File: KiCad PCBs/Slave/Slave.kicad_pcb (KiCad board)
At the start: 2 copper layers, 73 x 55.9 mm, 46 parts, among them J1 Screw_Terminal_01x02, J10 AVR-ISP-6, J11 Conn_01x06_Female, J12 Screw_Terminal_01x02, J13 Screw_Terminal_01x02, J14 Screw_Terminal_01x02, J15 Screw_Terminal_01x02, J16 Screw_Terminal_01x02, J2 Screw_Terminal_01x02, J3 Screw_Terminal_01x02, J4 Screw_Terminal_01x02, J5 Screw_Terminal_01x02, J6 Screw_Terminal_01x02, J7 Screw_Terminal_01x02, J8 Screw_Terminal_01x02, J9 Screw_Terminal_01x02, SW1 SW_DIP_x02, SW2 SW_DIP_x02, SW3 SW_MEC_5E, U1 ATmega328P-AU, U2 MAX487ESA+T, U3 ULN2003A, U5 AMS1117-5.0, Y1 Crystal_GND24

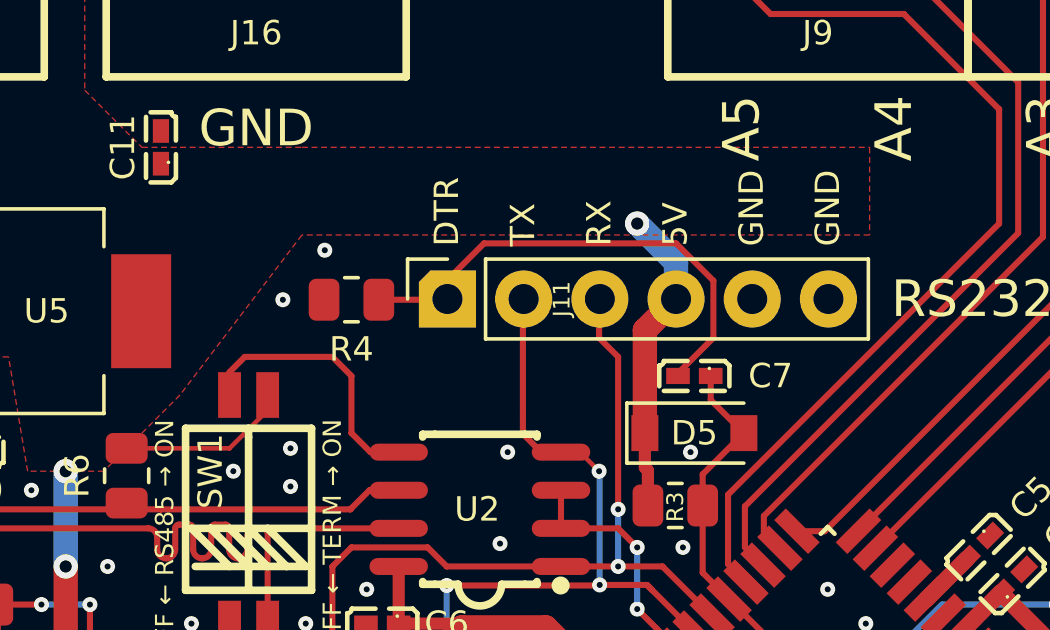
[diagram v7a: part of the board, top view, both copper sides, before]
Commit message: Removed unnecessary resistor
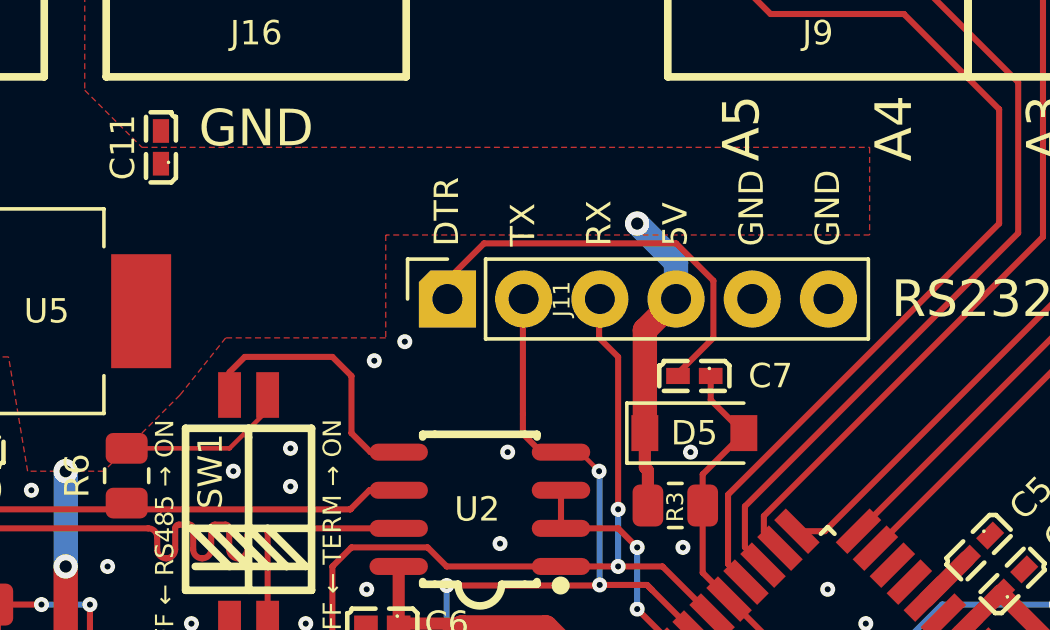
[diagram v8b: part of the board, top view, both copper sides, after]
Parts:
- removed R4: 1K, Resistor_SMD:R_0805_2012Metric
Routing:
- net FTDI_DTR: track 17.4 -> 14.7 mm
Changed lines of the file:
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@@
-    )
-  )
-  (footprint "Resistor_SMD:R_0805_2012Metric" (layer "F.Cu")
-    (at 133.985 91.4396 180)
-    (descr "Resistor SMD 0805 (2012 Metric), square (rectangular) end terminal, IPC_7351 nominal, (Body size source: IPC-SM-782 page 72, https://www.pcb-3d.com/wordpress/wp-content/uploads/ipc-sm-782a_amendment_1_and_2.pdf), generated with kicad-footprint-generator")
-    (tags "resistor")
-    (property "LCSC" "C17513")
-    (property "Sheetfile" "Slave.kicad_sch")
-    (property "Sheetname" "")
-    (attr smd)
-    (fp_text reference "R4" (at 0 -1.65 180) (layer "F.SilkS")
-      (effects (font (size 0.8128 0.8128) (thickness 0.127)))
-    )
-    (fp_text value "1K" (at 0 1.65 180) (layer "F.Fab")
-      (effects (font (size 1 1) (thickness 0.15)))
-    )
-    (fp_text user "${REFERENCE}" (at 0 0 180) (layer "F.Fab")
-      (effects (font (size 0.5 0.5) (thickness 0.08)))
-    )
-    (fp_line (start -0.227064 0.735) (end 0.227064 0.735) (layer "F.SilkS") (width 0.12))
-    (fp_line (start -0.227064 -0.735) (end 0.227064 -0.735) (layer "F.SilkS") (width 0.12))
-    (fp_line (start 1.68 0.95) (end -1.68 0.95) (layer "F.CrtYd") (width 0.05))
-    (fp_line (start 1.68 -0.95) (end 1.68 0.95) (layer "F.CrtYd") (width 0.05))
-    (fp_line (start -1.68 -0.95) (end 1.68 -0.95) (layer "F.CrtYd") (width 0.05))
-    (fp_line (start -1.68 0.95) (end -1.68 -0.95) (layer "F.CrtYd") (width 0.05))
-    (fp_line (start 1 0.625) (end -1 0.625) (layer "F.Fab") (width 0.1))
-    (fp_line (start 1 -0.625) (end 1 0.625) (layer "F.Fab") (width 0.1))
-    (fp_line (start -1 0.625) (end -1 -0.625) (layer "F.Fab") (width 0.1))
-    (fp_line (start -1 -0.625) (end 1 -0.625) (layer "F.Fab") (width 0.1))
-    (pad "1" smd roundrect (at -0.9125 0 180) (size 1.025 1.4) (layers "F.Cu" "F.Paste" "F.Mask") (roundrect_rratio 0.243902439)
-      (net 4 "FTDI_DTR") (pintype "passive"))
-    (pad "2" smd roundrect (at 0.9125 0 180) (size 1.025 1.4) (layers "F.Cu" "F.Paste" "F.Mask") (roundrect_rratio 0.243902439)
-      (net 45 "GND") (pintype "passive"))
-    (model "${KICAD6_3DMODEL_DIR}/Resistor_SMD.3dshapes/R_0805_2012Metric.wrl"
-      (offset (xyz 0 0 0))
-      (scale (xyz 1 1 1))
-      (rotate (xyz 0 0 0))
     )
   )
@@
   (segment (start 144.869915 93.890085) (end 146.05 92.71) (width 0.2032) (layer "F.Cu") (net 4))
   (segment (start 138.4046 89.5604) (end 137.185 90.78) (width 0.2032) (layer "F.Cu") (net 4))
-  (segment (start 137.185 91.44) (end 134.4954 91.44) (width 0.2032) (layer "F.Cu") (net 4))
   (segment (start 144.284696 112.487395) (end 144.285481 112.487395) (width 0.1524) (layer "F.Cu") (net 5))
   (segment (start 142.539506 113.945196) (end 141.958493 113.364183) (width 0.1524) (layer "F.Cu") (net 5))
@@
   (via (at 145.288 96.52) (size 0.5) (drill 0.2) (layers "F.Cu" "B.Cu") (free) (net 45))
   (via (at 147.193 103.759) (size 0.5) (drill 0.2) (layers "F.Cu" "B.Cu") (free) (net 45))
-  (via (at 133.096 89.789) (size 0.5) (drill 0.2) (layers "F.Cu" "B.Cu") (free) (net 45))
+  (via (at 135.763 92.837) (size 0.5) (drill 0.2) (layers "F.Cu" "B.Cu") (free) (net 45))
   (via (at 123.444 110.49) (size 0.5) (drill 0.2) (layers "F.Cu" "B.Cu") (free) (net 45))
   (via (at 150.114 120.523) (size 0.5) (drill 0.2) (layers "F.Cu" "B.Cu") (free) (net 45))
@@
   (via (at 154.178 113.538) (size 0.5) (drill 0.2) (layers "F.Cu" "B.Cu") (free) (net 45))
   (via (at 134.493 101.092) (size 0.5) (drill 0.2) (layers "F.Cu" "B.Cu") (free) (net 45))
-  (via (at 131.699 91.44) (size 0.5) (drill 0.2) (layers "F.Cu" "B.Cu") (free) (net 45))
+  (via (at 134.747 93.472) (size 0.5) (drill 0.2) (layers "F.Cu" "B.Cu") (free) (net 45))
   (via (at 119.507 96.139) (size 0.5) (drill 0.2) (layers "F.Cu" "B.Cu") (free) (net 45))
   (via (at 123.317 97.79) (size 0.5) (drill 0.2) (layers "F.Cu" "B.Cu") (free) (net 45))
@@
         (xy 151.257 86.36)
         (xy 151.257 89.281)
-        (xy 132.334 89.281)
+        (xy 135.128 89.281)
+        (xy 135.128 92.71)
+        (xy 129.794 92.71)
         (xy 128.27 94.615)
         (xy 125.73 97.155)
